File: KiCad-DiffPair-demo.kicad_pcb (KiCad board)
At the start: 4 copper layers, 60 x 30 mm, 5 parts, among them J1 HDMI_A, U1 IO_HDMI_LT6911UXC_QFN-64

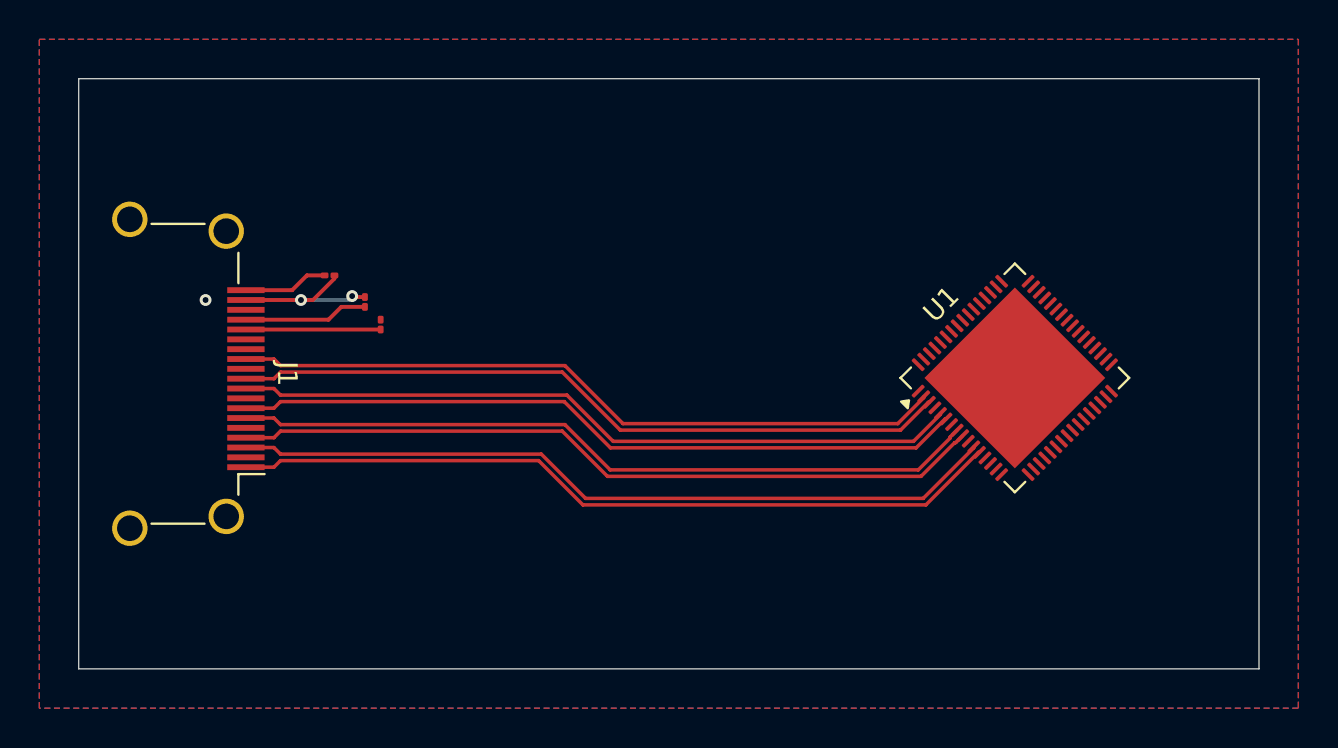
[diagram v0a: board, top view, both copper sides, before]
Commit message: Uprava diff pair, Uprava pravidla
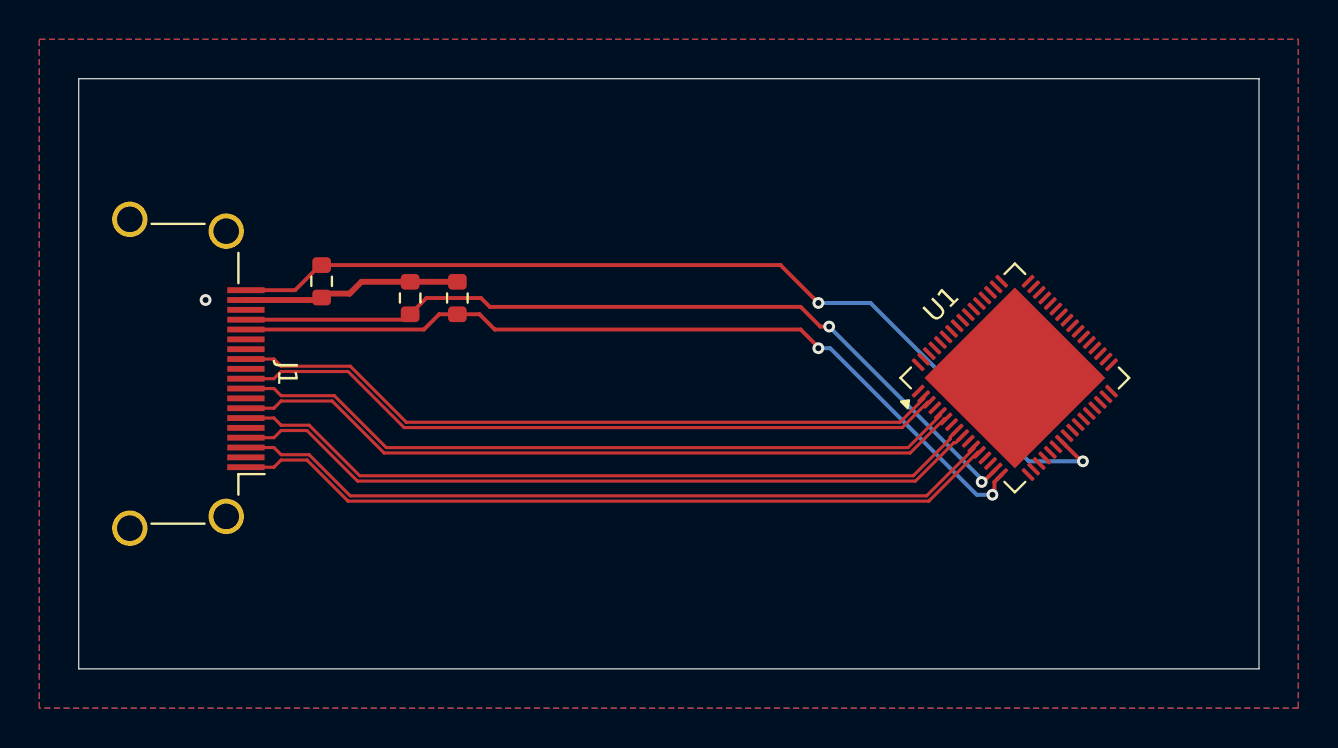
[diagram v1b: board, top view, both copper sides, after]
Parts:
- R1, R2, R3: footprint Resistor_SMD:R_01005_0402Metric -> Resistor_SMD:R_0603_1608Metric
- moved R1 4.13 mm to (19.2, -18.9)
- moved R2 2.31 mm to (16.9, -18.9)
- moved R3 0.50 mm to (12.3, -19.7), turned to 90 degrees
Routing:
- net /HDMI_HDP: track 4.31 -> 48.9 mm, vias 0 -> 2
- net /D_I2C_SDA: track 6.32 -> 42.8 mm, vias 0 -> 2
- net /D_I2C_SCL: track 6.85 -> 43.3 mm, vias 0 -> 2
- net +5V: track 8.47 -> 11.3 mm, vias 2 -> 0
